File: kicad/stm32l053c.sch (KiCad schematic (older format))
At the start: 56 parts, among them J1 Water_Level, J2 Motion, J3 Door, J4 Door_Led, J6 Pump, J7 BATTERY, P1 SWD, Q1 Q_NMOS_GSD, Q2 Q_PMOS_GSD, SW1 SW_Push_SPDT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

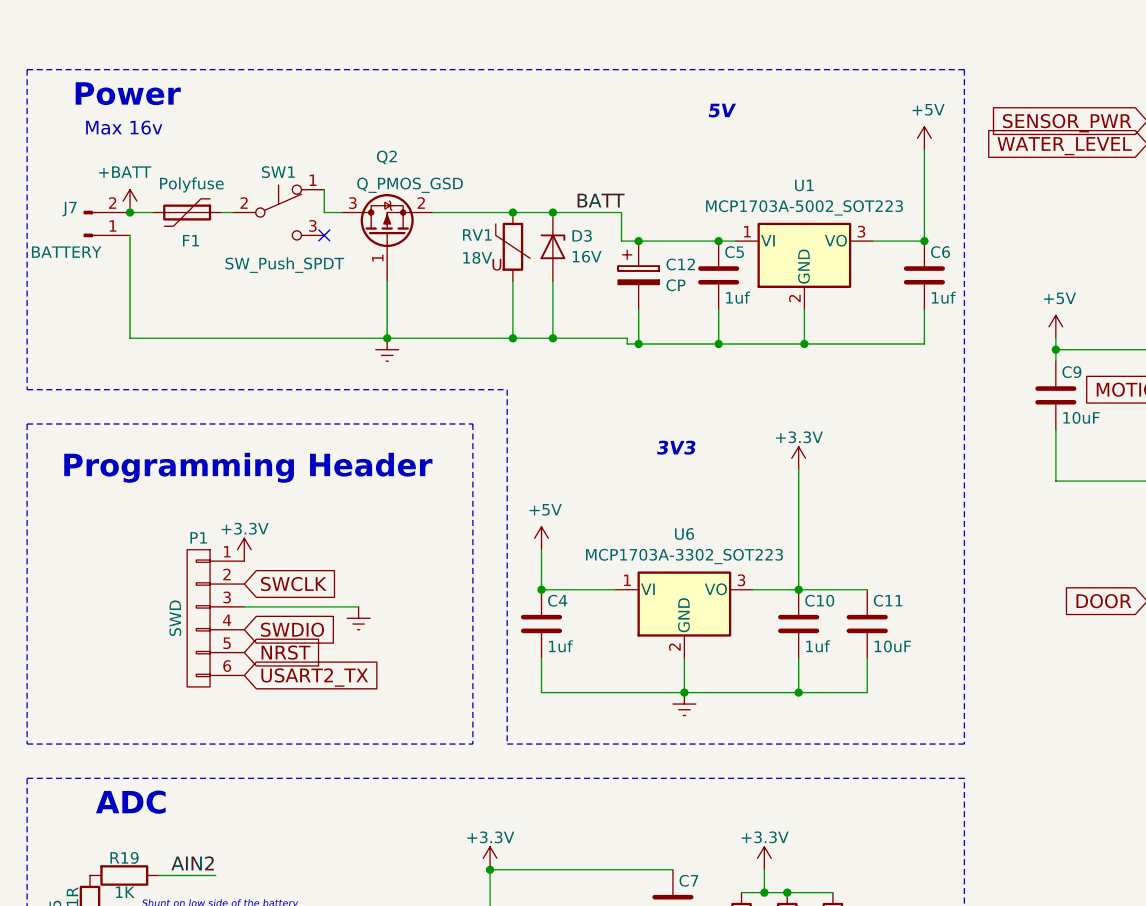
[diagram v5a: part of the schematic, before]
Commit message: Altenate 5V regulator
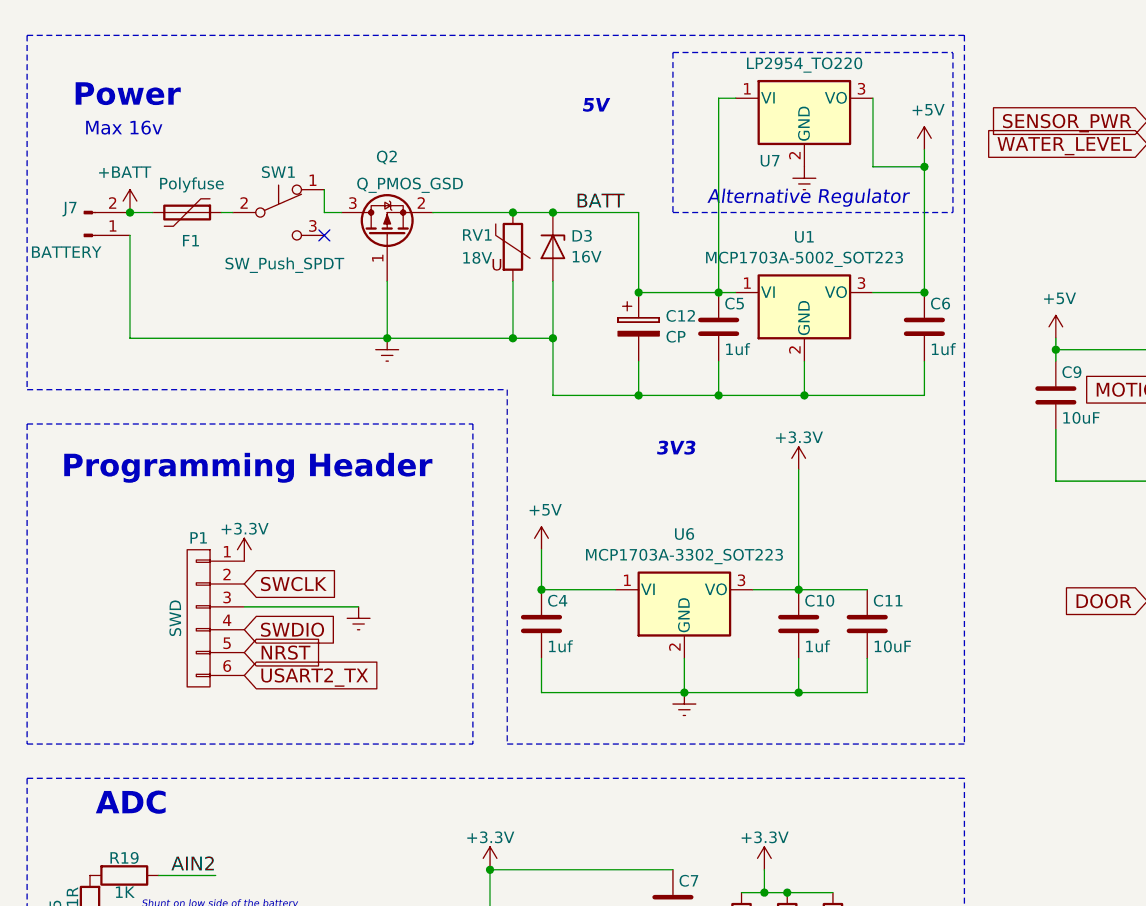
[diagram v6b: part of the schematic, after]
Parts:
- added U7: LP2954_TO220, Package_TO_SOT_THT:TO-220-3_Vertical, symbol Regulator_Linear:LM7805_TO220
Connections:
- net +5V: now also U7.3 (VO)
- net BATT: now also U7.1 (VI)
- net Earth: now also U7.2 (GND)
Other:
- note added: "Alternative Regulator"
- moved on the sheet: C12, C5, C6, U1
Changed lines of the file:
@@
 L stm32l053c-rescue:C C5
 U 1 1 59302470
-P 4000 1625
-F 0 "C5" H 4025 1725 50  0000 L CNN
-F 1 "1uf" H 4025 1525 50  0000 L CNN
-F 2 "Capacitor_SMD:C_0805_2012Metric_Pad1.15x1.40mm_HandSolder" H 4038 1475 50  0001 C CNN
-F 3 "" H 4000 1625 50  0001 C CNN
-	1    4000 1625
+P 4000 1850
+F 0 "C5" H 4025 1950 50  0000 L CNN
+F 1 "1uf" H 4025 1750 50  0000 L CNN
+F 2 "Capacitor_SMD:C_0805_2012Metric_Pad1.15x1.40mm_HandSolder" H 4038 1700 50  0001 C CNN
+F 3 "" H 4000 1850 50  0001 C CNN
+	1    4000 1850
 	1    0    0    -1
 $EndComp
@@
 L stm32l053c-rescue:C C6
 U 1 1 5930294B
-P 4900 1625
-F 0 "C6" H 4925 1725 50  0000 L CNN
-F 1 "1uf" H 4925 1525 50  0000 L CNN
-F 2 "Capacitor_SMD:C_0805_2012Metric_Pad1.15x1.40mm_HandSolder" H 4938 1475 50  0001 C CNN
-F 3 "" H 4900 1625 50  0001 C CNN
-	1    4900 1625
+P 4900 1850
+F 0 "C6" H 4925 1950 50  0000 L CNN
+F 1 "1uf" H 4925 1750 50  0000 L CNN
+F 2 "Capacitor_SMD:C_0805_2012Metric_Pad1.15x1.40mm_HandSolder" H 4938 1700 50  0001 C CNN
+F 3 "" H 4900 1850 50  0001 C CNN
+	1    4900 1850
 	1    0    0    -1
 $EndComp
@@
 	1675 6975 1450 6975
 Wire Notes Line
-	975  725  5075 725
+	975  575  5075 575
 Wire Notes Line
 	975  2275 975  3675
@@
 	3700 5025 4500 5025
 Wire Wire Line
-	4000 1925 4000 1775
-Wire Wire Line
-	4900 1925 4900 1775
-Connection ~ 4375 1925
+	4000 2150 4000 2000
+Wire Wire Line
+	4900 2150 4900 2000
+Connection ~ 4375 2150
 Wire Wire Line
 	3000 4225 3800 4225
@@
 Wire Notes Line
 	3075 3675 5075 3675
-Wire Notes Line
-	975  725  975  2125
 Wire Notes Line
 	2925 2275 2925 3675
@@
 	1    0    0    -1
 $EndComp
-Connection ~ 4900 1475
+Connection ~ 4900 1700
 $Comp
 L stm32l053c-rescue:R R10
@@
 USART2_RX
 Wire Wire Line
-	4375 1775 4375 1925
+	4375 2000 4375 2150
 Connection ~ 9725 6050
 $Comp
@@
 L Regulator_Linear:MCP1703A-5002_SOT223 U1
 U 1 1 5C257B3B
-P 4375 1475
-F 0 "U1" H 4375 1717 50  0000 C CNN
-F 1 "MCP1703A-5002_SOT223" H 4375 1626 50  0000 C CNN
-F 2 "Package_TO_SOT_SMD:SOT-223-3_TabPin2" H 4375 1675 50  0001 C CNN
-F 3 "http://ww1.microchip.com/downloads/en/DeviceDoc/20005122B.pdf" H 4375 1425 50  0001 C CNN
-	1    4375 1475
+P 4375 1700
+F 0 "U1" H 4375 1942 50  0000 C CNN
+F 1 "MCP1703A-5002_SOT223" H 4375 1851 50  0000 C CNN
+F 2 "Package_TO_SOT_SMD:SOT-223-3_TabPin2" H 4375 1900 50  0001 C CNN
+F 3 "http://ww1.microchip.com/downloads/en/DeviceDoc/20005122B.pdf" H 4375 1650 50  0001 C CNN
+	1    4375 1700
 	1    0    0    -1
 $EndComp
@@
 Text Notes 3725 2425 0    59   Italic 12
 3V3
-Text Notes 3950 950  0    59   Italic 12
+Text Notes 3400 925  0    59   Italic 12
 5V
 Wire Notes Line
@@
 Wire Notes Line
 	3075 2125 3075 3675
-Wire Notes Line
-	5075 725  5075 3675
 $Comp
 L power:+5V #PWR039
@@
 	1    0    0    -1
 $EndComp
-$Comp
-L Device:CP C12
-U 1 1 5C265527
-P 3650 1625
-F 0 "C12" H 3768 1671 50  0000 L CNN
-F 1 "CP" H 3768 1580 50  0000 L CNN
-F 2 "Capacitor_THT:CP_Radial_D8.0mm_P3.50mm" H 3688 1475 50  0001 C CNN
-F 3 "~" H 3650 1625 50  0001 C CNN
-	1    3650 1625
-	1    0    0    -1
-$EndComp
-Wire Wire Line
-	4000 1475 3650 1475
-Wire Wire Line
-	3650 1775 3650 1925
-Wire Wire Line
-	3650 1925 4000 1925
+Wire Wire Line
+	4000 1700 3650 1700
+Wire Wire Line
+	3650 2000 3650 2150
+Wire Wire Line
+	3650 2150 4000 2150
 $Comp
 L Connector:Conn_01x02_Female J6
@@
 $EndComp
 Wire Wire Line
-	4375 1925 4900 1925
-Wire Wire Line
-	4675 1475 4900 1475
+	4375 2150 4900 2150
+Wire Wire Line
+	4675 1700 4900 1700
 $Comp
 L Device:Polyfuse F1
@@
 	0    1    1    0
 $EndComp
-Connection ~ 3650 1475
 Wire Wire Line
 	4150 3000 4350 3000
@@
 	4350 3000 4350 2475
 Wire Wire Line
-	4900 1475 4900 1075
-Wire Wire Line
-	4075 1475 4000 1475
-Connection ~ 4000 1475
-Wire Wire Line
-	4000 1925 4375 1925
-Connection ~ 4000 1925
+	4075 1700 4000 1700
+Connection ~ 4000 1700
+Wire Wire Line
+	4000 2150 4375 2150
+Connection ~ 4000 2150
 NoConn ~ 8675 2700
-Wire Wire Line
-	3575 1475 3650 1475
 $Comp
 L Device:D_Zener D3
@@
 Connection ~ 3275 1350
 Wire Wire Line
-	3575 1350 3575 1475
-Wire Wire Line
-	3275 1350 3575 1350
-Wire Wire Line
 	5475 2300 5475 2525
 Wire Wire Line
@@
 Wire Wire Line
 	1425 1900 2550 1900
-Wire Wire Line
-	3275 1900 3600 1900
-Wire Wire Line
-	3600 1900 3600 1925
-Wire Wire Line
-	3600 1925 3650 1925
-Connection ~ 3275 1900
-Connection ~ 3650 1925
 Text Label 1800 4250 2    60   ~ 0
 AIN2
@@
 Wire Wire Line
 	2275 1350 2350 1350
+$Comp
+L Regulator_Linear:LM7805_TO220 U7
+U 1 1 5C2A2D54
+P 4375 850
+F 0 "U7" H 4225 575 50  0000 C CNN
+F 1 "LP2954_TO220" H 4375 1001 50  0000 C CNN
+F 2 "Package_TO_SOT_THT:TO-220-3_Vertical" H 4375 1075 50  0001 C CIN
+F 3 "http://www.fairchildsemi.com/ds/LM/LM7805.pdf" H 4375 800 50  0001 C CNN
+	1    4375 850
+	1    0    0    -1
+$EndComp
+Wire Wire Line
+	4075 850  4000 850
+Wire Wire Line
+	4000 850  4000 1700
+$Comp
+L power:Earth #PWR012
+U 1 1 5C2B142D
+P 4375 1150
+F 0 "#PWR012" H 4375 900 50  0001 C CNN
+F 1 "Earth" H 4375 1000 50  0001 C CNN
+F 2 "" H 4375 1150 50  0000 C CNN
+F 3 "" H 4375 1150 50  0000 C CNN
+	1    4375 1150
+	-1   0    0    -1
+$EndComp
+Wire Wire Line
+	4900 1075 4900 1150
+Wire Wire Line
+	4675 850  4675 1150
+Wire Wire Line
+	4675 1150 4900 1150
+Connection ~ 4900 1150
+Wire Wire Line
+	4900 1150 4900 1700
+Wire Notes Line
+	5075 575  5075 3675
+Wire Notes Line
+	975  575  975  2125
+Wire Notes Line
+	3800 650  3800 1350
+Wire Notes Line
+	3800 1350 5025 1350
+Wire Notes Line
+	5025 1350 5025 650
+Wire Notes Line
+	3800 650  5025 650
+Text Notes 3950 1325 0    60   Italic 0
+Alternative Regulator
+Connection ~ 3650 1700
+$Comp
+L Device:CP C12
+U 1 1 5C265527
+P 3650 1850
+F 0 "C12" H 3768 1896 50  0000 L CNN
+F 1 "CP" H 3768 1805 50  0000 L CNN
+F 2 "Capacitor_THT:CP_Radial_D8.0mm_P3.50mm" H 3688 1700 50  0001 C CNN
+F 3 "~" H 3650 1850 50  0001 C CNN
+	1    3650 1850
+	1    0    0    -1
+$EndComp
+Wire Wire Line
+	3275 1900 3275 2150
+Wire Wire Line
+	3275 2150 3650 2150
+Connection ~ 3275 1900
+Connection ~ 3650 2150
+Wire Wire Line
+	3275 1350 3650 1350
+Wire Wire Line
+	3650 1350 3650 1700
 $EndSCHEMATC

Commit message: Heatsinking for the 5V regulator
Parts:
- U1: footprint Package_TO_SOT_SMD:SOT-223-3_TabPin2 -> theapi:SOT-223-3_TabPin2_heatsink
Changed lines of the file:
@@
 F 0 "U1" H 4375 1942 50  0000 C CNN
 F 1 "MCP1703A-5002_SOT223" H 4375 1851 50  0000 C CNN
-F 2 "Package_TO_SOT_SMD:SOT-223-3_TabPin2" H 4375 1900 50  0001 C CNN
+F 2 "theapi:SOT-223-3_TabPin2_heatsink" H 4375 1900 50  0001 C CNN
 F 3 "http://ww1.microchip.com/downloads/en/DeviceDoc/20005122B.pdf" H 4375 1650 50  0001 C CNN
 	1    4375 1700

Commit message: Heatsinked vreg
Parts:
- U6: footprint Package_TO_SOT_SMD:SOT-223-3_TabPin2 -> theapi:SOT-223-3_TabPin2_heatsink
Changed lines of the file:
@@
 F 0 "U6" H 3850 3242 50  0000 C CNN
 F 1 "MCP1703A-3302_SOT223" H 3850 3151 50  0000 C CNN
-F 2 "Package_TO_SOT_SMD:SOT-223-3_TabPin2" H 3850 3200 50  0001 C CNN
+F 2 "theapi:SOT-223-3_TabPin2_heatsink" H 3850 3200 50  0001 C CNN
 F 3 "http://ww1.microchip.com/downloads/en/DeviceDoc/20005122B.pdf" H 3850 2950 50  0001 C CNN
 	1    3850 3000
